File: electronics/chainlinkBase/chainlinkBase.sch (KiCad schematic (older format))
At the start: 91 parts, among them J1 Power In, J10 12V SENSE, J11 Motor A, J12 Motor B, J13 Motor C, J14 Motor D, J15 Motor E, J16 Motor F, J17 Motor G, J18 Motor H, J19 Motor I, J2 UART, J20 Motor J, J21 Motor K, J22 Motor L, J3 SENSOR, J4 3.3v, J5 GND, J6 SR CHAIN IN, J7 SR CHAIN OUT, J8 RS485, J9 RS485, Q1 BSS138, Q2 BSS138, U11 INA219 Breakout Wide (blue), U16 LevelShifterModule, U18 TTGO_TDisplay, U19 74HC244, U2 SSD1306_I2C, U20 74HC165, U21 74HC165, U22 ST7789_80x160, U23 D1_32, U24 74HC595, U25 74HC595, U26 74HC595, U27 74HC595, U28 74HC595, U29 74HC595, U30 ST7789_240x240, U31 INA219 Breakout Narrow (purpl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, U32 SP485, U33 INA219BxD, U34 TPL7407LA, U35 TPL7407LA, U36 TPL7407LA, U37 TPL7407LA, U38 TPL7407LA, U39 TPL7407LA, U40 TPL7407LA

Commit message: Clean up schematic, initial component selection and schematic work
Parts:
- removed C10, C11, C12, C13, C14, C15, C16, C17, C18, C19, C20, C21, C22, C6, C7, C8, C9: 0.1uF, Capacitor_SMD:C_0805_2012Metric, symbol Device:C_Small
- removed C3: 100uF, Capacitor_SMD:CP_Elec_8x10.5, symbol Device:CP_Small
- removed H1, H2, H3, H4: MountingHole, MountingHole:MountingHole_4.3mm_M4_ISO7380_Pad, symbol Mechanical:MountingHole
- removed J10: 12V SENSE, TerminalBlock:TerminalBlock_bornier-2_P5.08mm, symbol Connector:Screw_Terminal_01x02
- removed J11: Motor A, JST_XH_Connectors:JST_XH_2-5mm_5pin, symbol Connector:Conn_01x05_Male
- removed J12: Motor B, JST_XH_Connectors:JST_XH_2-5mm_5pin, symbol Connector:Conn_01x05_Male
- removed J13: Motor C, JST_XH_Connectors:JST_XH_2-5mm_5pin, symbol Connector:Conn_01x05_Male
- removed J14: Motor D, JST_XH_Connectors:JST_XH_2-5mm_5pin, symbol Connector:Conn_01x05_Male
- removed J15: Motor E, JST_XH_Connectors:JST_XH_2-5mm_5pin, symbol Connector:Conn_01x05_Male
- removed J16: Motor F, JST_XH_Connectors:JST_XH_2-5mm_5pin, symbol Connector:Conn_01x05_Male
- removed J17: Motor G, JST_XH_Connectors:JST_XH_2-5mm_5pin, symbol Connector:Conn_01x05_Male
- removed J18: Motor H, JST_XH_Connectors:JST_XH_2-5mm_5pin, symbol Connector:Conn_01x05_Male
- removed J19: Motor I, JST_XH_Connectors:JST_XH_2-5mm_5pin, symbol Connector:Conn_01x05_Male
- removed J20: Motor J, JST_XH_Connectors:JST_XH_2-5mm_5pin, symbol Connector:Conn_01x05_Male
- removed J21: Motor K, JST_XH_Connectors:JST_XH_2-5mm_5pin, symbol Connector:Conn_01x05_Male
- removed J22: Motor L, JST_XH_Connectors:JST_XH_2-5mm_5pin, symbol Connector:Conn_01x05_Male
- removed J3: SENSOR, Connector_PinHeader_2.54mm:PinHeader_1x12_P2.54mm_Vertical, symbol Connector:Conn_01x12_Male
- removed J4: 3.3v, Connector_PinHeader_2.54mm:PinHeader_1x12_P2.54mm_Vertical, symbol Connector:Conn_01x12_Male
- removed J5: GND, Connector_PinHeader_2.54mm:PinHeader_1x12_P2.54mm_Vertical, symbol Connector:Conn_01x12_Male
- removed J6: SR CHAIN IN, Connector_PinSocket_2.54mm:PinSocket_1x06_P2.54mm_Vertical, symbol Connector:Screw_Terminal_01x06
- removed J7: SR CHAIN OUT, Connector_PinSocket_2.54mm:PinSocket_1x06_P2.54mm_Vertical, symbol Connector:Screw_Terminal_01x06
- removed JP2: RX BYPASS, Jumper:SolderJumper-2_P1.3mm_Open_TrianglePad1.0x1.5mm, symbol Jumper:SolderJumper_2_Open
- removed JP3: TX BYPASS, Jumper:SolderJumper-2_P1.3mm_Open_TrianglePad1.0x1.5mm, symbol Jumper:SolderJumper_2_Open
- removed JP4: A0, Jumper:SolderJumper-2_P1.3mm_Open_TrianglePad1.0x1.5mm, symbol Jumper:SolderJumper_2_Open
- removed JP5: A1, Jumper:SolderJumper-2_P1.3mm_Open_TrianglePad1.0x1.5mm, symbol Jumper:SolderJumper_2_Open
- removed Q2: BSS138, Package_TO_SOT_SMD:SOT-23, symbol Transistor_FET:BSS138
- removed R1, R14, R16, R17, R18: 10k, Resistor_SMD:R_0805_2012Metric, symbol Device:R_Small
- removed RN1, RN2, RN3: 47k, Resistor_SMD:R_Cat16-4, symbol Device:R_Pack04
- removed U11: INA219 Breakout Wide (blue), INA219:INA219_LARGE, symbol INA219_Breakout:INA219_Breakout
- removed U16: LevelShifterModule, LevelShifterModule:LevelShifterModule, symbol LevelShifterModule:LevelShifterModule
- removed U19: 74HC244, Package_SO:TSSOP-20_4.4x6.5mm_P0.65mm, symbol 74xx:74HC244
- removed U2: SSD1306_I2C, Connector_PinSocket_2.54mm:PinSocket_1x04_P2.54mm_Vertical, symbol oled:SSD1306_I2C
- removed U20, U21: 74HC165, Package_SO:SOIC-16_3.9x9.9mm_P1.27mm, symbol 74HC165_2:74HC165
- removed U22: ST7789_80x160, ST7789:ST7789_80x160, symbol LCD:ST7789_80x160
- removed U23: D1_32, ESP32:D1_32, symbol ESP32Modules:D1_32
- removed U24, U25, U26, U27, U28, U29: 74HC595, Package_SO:SOIC-16_3.9x9.9mm_P1.27mm, symbol 74xx:74HC595
- removed U30: ST7789_240x240, ST7789:ST7789_240x240, symbol LCD:ST7789_240x240
- removed U31: INA219 Breakout Narrow (purple), INA219:INA219_SMALL, symbol INA219_Breakout:INA219_Breakout
- removed U34, U35, U36, U37, U38, U39, U40: TPL7407LA, Package_SO:SOIC-16_3.9x9.9mm_P1.27mm, symbol Transistor_Array:ULN2003A
- added C? (x11): 0.1uF, symbol Device:C_Small
- added C? (x10): 1uF, symbol Device:C_Small
- added C? (x5): 0.1uF, Capacitor_SMD:C_0805_2012Metric, symbol Device:C_Small
- added D? (x5): LED_Small, symbol Device:LED_Small
- added D? (x5): WS2812B, LED_SMD:LED_WS2812B_PLCC4_5.0x5.0mm_P3.2mm, symbol LED:WS2812B
- added F? (x5): Fuse Holder BK-6013, symbol Device:Fuse
- added J? (x5): CHANNEL POWER, symbol Connector:Screw_Terminal_01x03
- added R? (x5): 220, symbol Device:R_Small
- added R? (x3): 10k, symbol Device:R_Small
- added R? (x4): 0.01R 1% 1W, Resistor_SMD:R_2512_6332Metric_Pad1.52x3.35mm_HandSolder, symbol Device:R_Small
- added U?: MCP23017_SO, Package_SO:SOIC-28W_7.5x17.9mm_P1.27mm, symbol Interface_Expansion:MCP23017_SO
- added U? (x5): NCP45560-H, symbol NCP45560:NCP45560
- added U?: TPL7407L, symbol Transistor_Array:ULN2003A
- added U? (x4): INA219BxD, Package_SO:SOIC-8_3.9x4.9mm_P1.27mm, symbol Analog_ADC:INA219BxD
- added U?: SN74LV1T34DBV, Package_TO_SOT_SMD:SOT-23-5, symbol Logic_LevelTranslator:SN74LV1T34DBV
- C?: renamed from C4; value 10uF -> 100uF
- R?: renamed from R19; value 0.1R 1% 1/2 W -> 0.01R 1% 1W
- renumbered C1 to C?, C2 to C?, C5 to C?, J1 to J?, J2 to J?, J8 to J?, J9 to J?, Q1 to Q?, R13 to R?, R15 to R?, U18 to U?, U32 to U?, U33 to U?
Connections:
- net labels added: LATCH, MASTER_EN, MCP_RESET, OUT0_EN, OUT0_PG, OUT1_EN, OUT1_PG, OUT2_EN, OUT2_PG, OUT3_EN, OUT3_PG, OUT4_EN, OUT4_PG, RELAY_MASTER, RELAY_OUT0, RELAY_OUT1, RELAY_OUT2, RELAY_OUT3, RELAY_OUT4, RGB_LEDS
- net labels removed: +12V_Monitored, CLOCK_IN, DISP_BLK, DISP_CLK, DISP_CS, DISP_DC, DISP_MOSI, DISP_RES, MOTOR_A_PHASE_A, MOTOR_A_PHASE_B, MOTOR_A_PHASE_C, MOTOR_A_PHASE_D, MOTOR_B_PHASE_A, MOTOR_B_PHASE_B, MOTOR_B_PHASE_C, MOTOR_B_PHASE_D, MOTOR_C_PHASE_A, MOTOR_C_PHASE_B, MOTOR_C_PHASE_C, MOTOR_C_PHASE_D, MOTOR_DATA_IN, MOTOR_DATA_OUT, MOTOR_D_PHASE_A, MOTOR_D_PHASE_B, MOTOR_D_PHASE_C, MOTOR_D_PHASE_D, MOTOR_E_PHASE_A, MOTOR_E_PHASE_B, MOTOR_E_PHASE_C, MOTOR_E_PHASE_D, MOTOR_F_PHASE_A, MOTOR_F_PHASE_B, MOTOR_F_PHASE_C, MOTOR_F_PHASE_D, MOTOR_G_PHASE_A, MOTOR_G_PHASE_B, MOTOR_G_PHASE_C, MOTOR_G_PHASE_D, MOTOR_H_PHASE_A, MOTOR_H_PHASE_B, MOTOR_H_PHASE_C, MOTOR_H_PHASE_D, MOTOR_I_PHASE_A, MOTOR_I_PHASE_B, MOTOR_I_PHASE_C, MOTOR_I_PHASE_D, MOTOR_J_PHASE_A, MOTOR_J_PHASE_B, MOTOR_J_PHASE_C, MOTOR_J_PHASE_D, MOTOR_K_PHASE_A, MOTOR_K_PHASE_B, MOTOR_K_PHASE_C, MOTOR_K_PHASE_D, MOTOR_LATCH, MOTOR_LATCH_IN, MOTOR_L_PHASE_A, MOTOR_L_PHASE_B, MOTOR_L_PHASE_C, MOTOR_L_PHASE_D, MOTOR_OE, MOTOR_OE_IN, OUT_A_PHASE_A, OUT_A_PHASE_B, OUT_A_PHASE_C, OUT_A_PHASE_D, OUT_B_PHASE_A, OUT_B_PHASE_B, OUT_B_PHASE_C, OUT_B_PHASE_D, OUT_C_PHASE_A, OUT_C_PHASE_B, OUT_C_PHASE_C, OUT_C_PHASE_D, OUT_D_PHASE_A, OUT_D_PHASE_B, OUT_D_PHASE_C, OUT_D_PHASE_D, OUT_E_PHASE_A, OUT_E_PHASE_B, OUT_E_PHASE_C, OUT_E_PHASE_D, OUT_F_PHASE_A, OUT_F_PHASE_B, OUT_F_PHASE_C, OUT_F_PHASE_D, OUT_G_PHASE_A, OUT_G_PHASE_B, OUT_G_PHASE_C, OUT_G_PHASE_D, OUT_H_PHASE_A, OUT_H_PHASE_B, OUT_H_PHASE_C, OUT_H_PHASE_D, OUT_I_PHASE_A, OUT_I_PHASE_B, OUT_I_PHASE_C, OUT_I_PHASE_D, OUT_J_PHASE_A, OUT_J_PHASE_B, OUT_J_PHASE_C, OUT_J_PHASE_D, OUT_K_PHASE_A, OUT_K_PHASE_B, OUT_K_PHASE_C, OUT_K_PHASE_D, OUT_L_PHASE_A, OUT_L_PHASE_B, OUT_L_PHASE_C, OUT_L_PHASE_D, SENSOR_A, SENSOR_B, SENSOR_C, SENSOR_D, SENSOR_DATA_CHAIN, SENSOR_DATA_IN, SENSOR_E, SENSOR_F, SENSOR_G, SENSOR_H, SENSOR_I, SENSOR_J, SENSOR_K, SENSOR_L, SENSOR_LATCH, SENSOR_LATCH_IN
- wire segments 740 -> 442
- no-connect marks 35 -> 10
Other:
- note added: "IN"
- note added: "OUT SWITCHED"
- note added: "PRE-SWITCH"
- note added: "Red, 10A, 0.008 Ohm typ\ne.g. 0297010.WXNV"
- note added: "Relay Driver"
- note added: "e.g. CFG0612-FX-R010ELF"
- note removed: "3A minimum rating, 5A+ preferred"
- note removed: "Configuration options:\n\nMega 2560: DNP U16; External RX/TX = 5V; do not use JP2/JP3\n\nESP32/ESP8266:\n For 5V RX/TX: Use U16; do not use JP2/JP3\n For 3.3V RX/TX: DNP U16; set JP2 and JP3"
- note removed: "ESP32/ESP8266 IO Support"
- note removed: "For compatibility with ESP8266, all critical IO\nuses the inner pins; optional IO (e.g. display)\ncan use the outer pins (only present for ESP32\nmodules)"
- note removed: "MCU Option 2: TTGO T-Display (ESP32)"
- note removed: "MCU Option 3: ESP32/ESP8266 D1 Mini"
- note removed: "Optional: Current sense\n\nTo omit, install a jumper wire across 12V SENSE.\n\nThere are 3 options:\n- "Adafruit-style" wide module (blue)\n- narrow module (purple)\n- populate IC and supporting components directly on PCB\n\nFor modules, install wires from screw terminals\non the module to 12V SENSE screw terminals: \nVIN+ to VIN+ & VIN- to VIN-\n\n12V SENSE is unused with populated IC."
- note removed: "Optional: RS485 comms/UART voltage shifting"
- note removed: "Optional: Shift register chaining support"
- note removed: "RS485 Requires 5V RX/TX - for ESP32/ESP8266 must use level shifter"
- note removed: "Sensor Connectors"
- note removed: "TODO: bypass capacitors"
- note removed: "VIN- and VIN+ are not connected via module\nheaders because max current is near the limit\nof pin headers. Use screw terminals instead."
- moved on the sheet: C?, J?, R?, U?

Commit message: checkpoint - more component selection and schematic work
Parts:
- removed C? (x6): 0.1uF, Capacitor_SMD:C_0805_2012Metric, symbol Device:C_Small
- removed C? (x4): 0.1uF, symbol Device:C_Small
- removed C? (x8): 1uF, symbol Device:C_Small
- removed C?: 100uF, Capacitor_SMD:CP_Elec_4x5.4, symbol Device:CP_Small
- removed D? (x4): LED_Small, symbol Device:LED_Small
- removed F? (x4): Fuse Holder BK-6013, symbol Device:Fuse
- removed J?: Power In, TerminalBlock:TerminalBlock_bornier-4_P5.08mm, symbol Connector:Screw_Terminal_01x04
- removed J? (x5): CHANNEL POWER, symbol Connector:Screw_Terminal_01x03
- removed Q?: BSS138, Package_TO_SOT_SMD:SOT-23, symbol Transistor_FET:BSS138
- removed R? (x4): 220, symbol Device:R_Small
- removed R? (x4): 0.01R 1% 1W, Resistor_SMD:R_2512_6332Metric_Pad1.52x3.35mm_HandSolder, symbol Device:R_Small
- removed R? (x2): 10k, Resistor_SMD:R_0805_2012Metric, symbol Device:R_Small
- removed U? (x4): INA219BxD, Package_SO:SOIC-8_3.9x4.9mm_P1.27mm, symbol Analog_ADC:INA219BxD
- removed U? (x4): NCP45560-H, symbol NCP45560:NCP45560
- removed U?: SN74LV1T34DBV, Package_TO_SOT_SMD:SOT-23-5, symbol Logic_LevelTranslator:SN74LV1T34DBV
- added C1, C4: 47uF, symbol Device:CP_Small
- added C11, C12, C17, C18, C19, C20, C25, C26: 1uF, Capacitor_SMD:C_0805_2012Metric, symbol Device:C_Small
- added C13, C14, C15, C16, C21, C23, C24, C33, C6, C8: 0.1uF, Capacitor_SMD:C_0805_2012Metric, symbol Device:C_Small
- added C2, C3: 4.7uF, Capacitor_SMD:C_0805_2012Metric, symbol Device:C_Small
- added D11: WS2812B, LED_SMD:LED_WS2812B_PLCC4_5.0x5.0mm_P3.2mm, symbol LED:WS2812B
- added D2, D3, D4, D5: LED_Small, LED_SMD:LED_0805_2012Metric, symbol Device:LED_Small
- added F2, F3, F4, F5: Fuse Holder BK-6013, symbol Device:Fuse
- added J1: Power In, TerminalBlock:TerminalBlock_bornier-2_P5.08mm, symbol Connector:Screw_Terminal_01x02
- added J10, J11, J12: Output, TerminalBlock:TerminalBlock_bornier-2_P5.08mm, symbol Connector:Screw_Terminal_01x02
- added J13, J2, J3, J4, J5: CHANNEL, TerminalBlock:TerminalBlock_bornier-2_P5.08mm, symbol Connector:Screw_Terminal_01x02
- added J8: Logic Power Out, TerminalBlock:TerminalBlock_bornier-2_P5.08mm, symbol Connector:Screw_Terminal_01x02
- added R10, R11, R16, R2: 0.01R 1% 1W, Resistor_SMD:R_0612_1632Metric, symbol Device:R_Small
- added R12, R13, R17, R5, R6: 10k, Resistor_SMD:R_0805_2012Metric, symbol Device:R_Small
- added R14, R15, R18, R8: 220, Resistor_SMD:R_0805_2012Metric, symbol Device:R_Small
- added SW1: SW_DIP_x04, Button_Switch_SMD:SW_DIP_SPSTx04_Slide_Omron_A6S-410x_W8.9mm_P2.54mm, symbol Switch:SW_DIP_x04
- added U1: AP7361C-33E, Package_TO_SOT_SMD:SOT-223-3_TabPin2, symbol Regulator_Linear:AP7361C-33E
- added U10, U15, U4, U9: INA219BxD, Package_SO:SOIC-8_3.9x4.9mm_P1.27mm, symbol Analog_ADC:INA219BxD
- added U11, U12, U16, U6: NCP45560-H, Package_DFN_QFN:DFN-12-1EP_3x3mm_P0.5mm_EP2.05x2.86mm, symbol NCP45560:NCP45560
- added U13, U17: SN74LV1T34DBV, Package_TO_SOT_SMD:SOT-23-5, symbol Logic_LevelTranslator:SN74LV1T34DBV
- C10, C27, C28, C29, C30, C31, C32, C7, C9: renamed from C?; footprint (none) -> Capacitor_SMD:C_0805_2012Metric
- D1: renamed from D?; footprint (none) -> LED_SMD:LED_0805_2012Metric
- R1: renamed from R?; footprint Resistor_SMD:R_2512_6332Metric_Pad1.52x3.35mm_HandSolder -> Resistor_SMD:R_0612_1632Metric
- R3, R4: renamed from R?; value 10k -> 2.2k; footprint (none) -> Resistor_SMD:R_0805_2012Metric
- R7, R9: renamed from R?; footprint (none) -> Resistor_SMD:R_0805_2012Metric
- U2: renamed from U?; value TPL7407L -> TPL7407LA; footprint (none) -> ModifiedSymbols:SOIC-16_3.9x9.9mm_P1.27mm_silk; DK# (none) -> 296-51862-1-ND
- U3: renamed from U?; DK# (none) -> 296-27899-1-ND
- U5: renamed from U?; footprint (none) -> Package_DFN_QFN:DFN-12-1EP_3x3mm_P0.5mm_EP2.05x2.86mm
- U8: renamed from U?; value MCP23017_SO -> MCP23017_SS; footprint Package_SO:SOIC-28W_7.5x17.9mm_P1.27mm -> Package_SO:SSOP-28_5.3x10.2mm_P0.65mm; symbol Interface_Expansion:MCP23017_SO -> Interface_Expansion:MCP23017_SS; DK# (none) -> MCP23017-E/SS-ND
- gave numbers to parts that had none: 13
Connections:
- net labels added: 3V3_EXT, ADDR_0, ADDR_1, ADDR_2, ADDR_3, MCP_INT, RGB_LEDS_3V3
- net labels removed: +12V, RX_EXT, TX_EXT
- wire segments 442 -> 507
- no-connect marks 10 -> 14
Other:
- note added: "3.3V supply for Chainlink Driver logic.\nMax ~~20mA per Chainlink Driver when all 6 LEDs are on."
- note added: "I2C ADDR: 0x27"
- note added: "I2C ADDR: 0x40"
- note added: "I2C ADDR: 0x41"
- note added: "I2C ADDR: 0x42"
- note added: "I2C ADDR: 0x43"
- note added: "I2C ADDR: 0x44"
- note added: "Level-shift 3.3V to 5V for WS2812b LEDs"
- note added: "SP485 accepts 3.3v inputs (2v VIH), so level-shifter is only needed for receive 5v -> 3.3v"
- note removed: "Connectors"
- note removed: "PRE-SWITCH"
- moved on the sheet: C27, C28, C29, C30, C31, C32, D10, D6, D7, D8, D9, J9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

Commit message: Switch to VN7007ALHTR for load switches
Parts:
- removed C13, C14, C23, C24: 0.1uF, Capacitor_SMD:C_0805_2012Metric, symbol Device:C_Small
- removed C17, C18, C19, C20, C25, C26: 1uF, Capacitor_SMD:C_0805_2012Metric, symbol Device:C_Small
- removed J13: CHANNEL, TerminalBlock:TerminalBlock_bornier-2_P5.08mm, symbol Connector:Screw_Terminal_01x02
- removed R13, R6: 10k, Resistor_SMD:R_0805_2012Metric, symbol Device:R_Small
- removed U11, U12, U16, U5, U6: NCP45560-H, Package_DFN_QFN:DFN-12-1EP_3x3mm_P0.5mm_EP2.05x2.86mm, symbol NCP45560:NCP45560
- added J14, J6: CHANNEL, TerminalBlock:TerminalBlock_bornier-2_P5.08mm, symbol Connector:Screw_Terminal_01x02
- added R19, R25, R26, R4, R7: 15k, Resistor_SMD:R_0805_2012Metric, symbol Device:R_Small
- added R20, R21, R27: 220, Resistor_SMD:R_0805_2012Metric, symbol Device:R_Small
- added R22, R23, R28: 1k, Resistor_SMD:R_0805_2012Metric, symbol Device:R_Small
- added R24: 0.01R 1% 1W, Resistor_SMD:R_0612_1632Metric, symbol Device:R_Small
- added U11, U12, U16, U5, U6: VN7007ALH, VN7007ALHTR:VN7007ALHTR, symbol VN7007ALHTR:VN7007ALH-LoadSwitches
- C10, C11, C12, C9: value 1uF -> 0.1uF
- J4: value CHANNEL -> RELAY
- R10: value 0.01R 1% 1W -> 220; footprint Resistor_SMD:R_0612_1632Metric -> Resistor_SMD:R_0805_2012Metric
- R11: value 0.01R 1% 1W -> 1k; footprint Resistor_SMD:R_0612_1632Metric -> Resistor_SMD:R_0805_2012Metric
- R12: value 10k -> 1k
- R14, R15: value 220 -> 0.01R 1% 1W; footprint Resistor_SMD:R_0805_2012Metric -> Resistor_SMD:R_0612_1632Metric
- R16: value 0.01R 1% 1W -> 15k; footprint Resistor_SMD:R_0612_1632Metric -> Resistor_SMD:R_0805_2012Metric
- R17: value 10k -> 15k
- R18, R8: value 220 -> 15k
- R3: renamed from R5; value 10k -> 15k
- R5: renamed from R3; value 2.2k -> 1k
- R6: renamed from R4; value 2.2k -> 1k
- U10, U15, U4, U9: DK# (none) -> 296-27899-1-ND
- renumbered C21 to C13, C22 to C14, C27 to C17, C28 to C18, C29 to C19, C30 to C20, C31 to C21, C32 to C22, C33 to C23, J9 to J10, J10 to J11, J11 to J12, J12 to J13, J6 to J7, J7 to J8, J8 to J9, R9 to R13, R7 to R9
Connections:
- net labels removed: RELAY_OUT0, RELAY_OUT1, RELAY_OUT2, RELAY_OUT3, RELAY_OUT4
- wire segments 507 -> 435
- no-connect marks 14 -> 9
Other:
- moved on the sheet: C7, D1, R3, R9

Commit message: More progress on schematic and footprints
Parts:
- added D12, D13, D14, D15, D16: Red, LED_SMD:LED_0805_2012Metric, symbol Device:LED_Small
- added R29, R30, R31, R32, R33: 2k, Resistor_SMD:R_0805_2012Metric, symbol Device:R_Small
- D1, D2, D3, D4, D5: value LED_Small -> Red
- F1, F2, F3, F4, F5: footprint (none) -> BK-6013:BK-6013; DK# (none) -> BK-6013-ND
- J1, J11, J12, J13, J14, J2, J3, J4, J5, J6, J7, J8, J9: footprint TerminalBlock:TerminalBlock_bornier-2_P5.08mm -> ScrewTerminals:EB147A-02-D; DK# (none) -> EB147A-02-D
- J10: footprint TerminalBlock:TerminalBlock_bornier-3_P5.08mm -> ScrewTerminals:C72334_WJ500V-5.08-3P; DK# (none) -> EB147A-03-D
- R1, R14, R15, R2, R24: DK# (none) -> CFG0612-FX-R010ELFCT-ND
- U11, U12, U16, U5, U6: symbol VN7007ALHTR:VN7007ALH-LoadSwitches -> VN7007ALHTR:VN7007ALH
- U2: value TPL7407LA -> TPL7407L
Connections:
- net labels removed: OUT0_PG, OUT1_PG, OUT2_PG, OUT3_PG, OUT4_PG
- wire segments 435 -> 450
- no-connect marks 9 -> 24

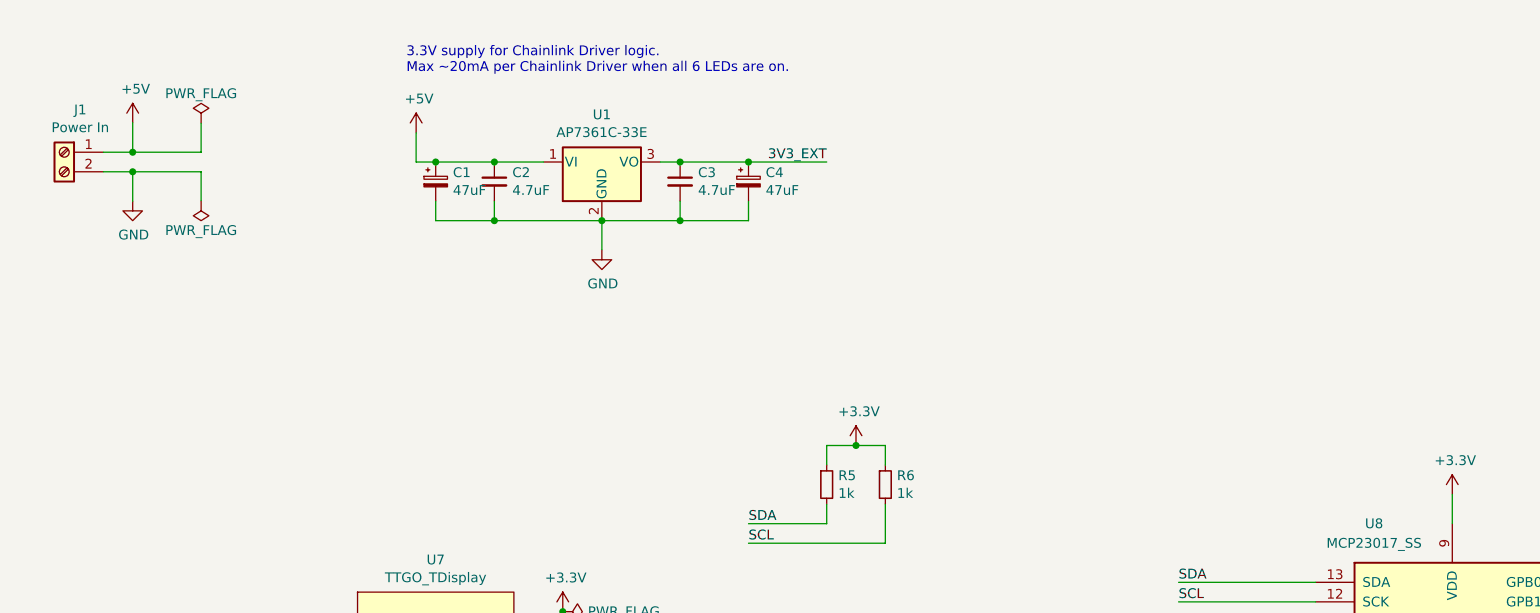
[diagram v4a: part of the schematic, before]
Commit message: Add buck option for power
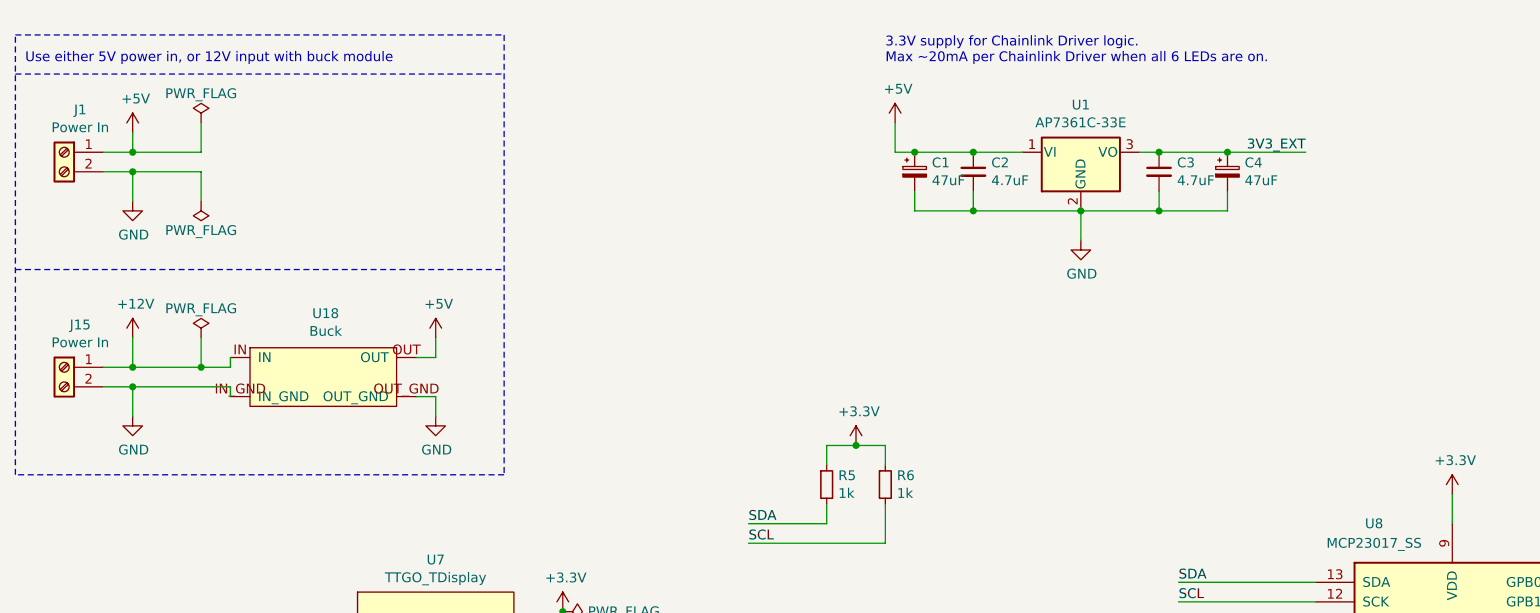
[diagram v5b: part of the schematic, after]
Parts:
- added J15: Power In, ScrewTerminals:EB147A-02-D, symbol Connector:Screw_Terminal_01x02
- added U18: Buck, Buck:BuckModule, symbol BuckModule:Buck
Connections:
- net +5V: now also U18.OUT
- net GND: now also J15.2 (Pin_2), U18.IN_GND, U18.OUT_GND
- new net +12V: J15.1 (Pin_1), U18.IN
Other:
- note added: "Use either 5V power in, or 12V input with buck module"
- moved on the sheet: C1, C2, C3, C4, U1

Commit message: Single channel layout
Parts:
- removed C10, C11, C12, C15, C16, C5, C6, C7, C8, C9: 0.1uF, Capacitor_SMD:C_0805_2012Metric, symbol Device:C_Small
- removed D1, D12, D13, D14, D15, D16, D2, D3, D4, D5: Red, LED_SMD:LED_0805_2012Metric, symbol Device:LED_Small
- removed F1, F2, F3, F4, F5: Fuse Holder BK-6013, BK-6013:BK-6013, symbol Device:Fuse
- removed J14, J2, J3, J5, J6: CHANNEL, ScrewTerminals:EB147A-02-D, symbol Connector:Screw_Terminal_01x02
- removed R1, R14, R15, R2, R24: 0.01R 1% 1W, Resistor_SMD:R_0612_1632Metric, symbol Device:R_Small
- removed R10, R20, R21, R27, R9: 220, Resistor_SMD:R_0805_2012Metric, symbol Device:R_Small
- removed R11, R12, R22, R23, R28: 1k, Resistor_SMD:R_0805_2012Metric, symbol Device:R_Small
- removed R16, R17, R18, R19, R25, R26, R3, R4, R7, R8: 15k, Resistor_SMD:R_0805_2012Metric, symbol Device:R_Small
- removed R29, R30, R31, R32, R33: 2k, Resistor_SMD:R_0805_2012Metric, symbol Device:R_Small
- removed U10, U15, U3, U4, U9: INA219BxD, Package_SO:SOIC-8_3.9x4.9mm_P1.27mm, symbol Analog_ADC:INA219BxD
- removed U11, U12, U16, U5, U6: VN7007ALH, VN7007ALHTR:VN7007ALHTR, symbol VN7007ALHTR:VN7007ALH
- added D107: 2A 500mV, Diode_SMD:D_SOD-128, symbol Device:D_Schottky_Small
- added H101, H102, H103, H104: MountingHole_Pad, MountingHole:MountingHole_3.2mm_M3_ISO7380_Pad, symbol Mechanical:MountingHole_Pad
- added JP101: LEDs, Connector_PinHeader_2.54mm:PinHeader_1x02_P2.54mm_Vertical, symbol Device:Jumper_NO_Small
- C101: renamed from C1; footprint (none) -> Capacitor_SMD:CP_Elec_6.3x5.4; DK# (none) -> 732-8508-1-ND
- C104: renamed from C4; footprint (none) -> Capacitor_SMD:CP_Elec_6.3x5.4; DK# (none) -> 732-8508-1-ND
- J101: renamed from J1; footprint ScrewTerminals:EB147A-02-D -> ScrewTerminals:Generic-5.08-2P
- J102: renamed from J4; footprint ScrewTerminals:EB147A-02-D -> ScrewTerminals:Generic-5.08-2P
- J103: renamed from J15; footprint ScrewTerminals:EB147A-02-D -> ScrewTerminals:Generic-5.08-2P
- J104: renamed from J7; footprint ScrewTerminals:EB147A-02-D -> ScrewTerminals:Generic-5.08-2P
- J105: renamed from J8; footprint ScrewTerminals:EB147A-02-D -> ScrewTerminals:Generic-5.08-2P
- J106: renamed from J9; footprint ScrewTerminals:EB147A-02-D -> ScrewTerminals:Generic-5.08-2P
- J107: renamed from J10; footprint ScrewTerminals:C72334_WJ500V-5.08-3P -> ScrewTerminals:Generic-5.08-3P
- J108: renamed from J11; footprint ScrewTerminals:EB147A-02-D -> ScrewTerminals:Generic-5.08-2P
- J109: renamed from J12; footprint ScrewTerminals:EB147A-02-D -> ScrewTerminals:Generic-5.08-2P
- J110: renamed from J13; footprint ScrewTerminals:EB147A-02-D -> ScrewTerminals:Generic-5.08-2P
- renumbered C2 to C102, C3 to C103, C13 to C105, C14 to C106, C17 to C107, C18 to C108, C19 to C109, C20 to C110, C21 to C111, C22 to C112, C23 to C113, D6 to D101, D7 to D102, D8 to D103, D9 to D104, D10 to D105, D11 to D106, R5 to R101, R6 to R102, R13 to R103, SW1 to SW101, U1 to U101, U2 to U102, U18 to U103, U7 to U104, U8 to U105, U13 to U106, U14 to U107, U17 to U108
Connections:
- net +5V: now also D107.1 (K); no longer U103.OUT
- net GND: now also H101.1, H102.1, H103.1, H104.1, JP101.2
- new net: D107.2 (A), U103.OUT
- new net LED_GND: JP101.1
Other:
- note added: "Table1. INA219 Address Pins and Slave Addresses\nA1 A0 SLAVE ADDRESS\nGND GND 1000000\nGND VS+ 1000001\nGND SDA 1000010\nGND SCL 1000011\nVS+ GND 1000100\nVS+ VS+ 1000101\nVS+ SDA 1000110\nVS+ SCL 1000111\nSDA GND 1001000\nSDA VS+ 1001001\nSDA SDA 1001010\nSDA SCL 1001011\nSCL GND 1001100\nSCL VS+ 1001101\nSCL SDA 1001110\nSCL SCL 1001111"
- note removed: "IN"
- note removed: "OUT SWITCHED"
- note removed: "Red, 10A, 0.008 Ohm typ\ne.g. 0297010.WXNV"
- note removed: "e.g. CFG0612-FX-R010ELF"
- moved on the sheet: J102, U102
